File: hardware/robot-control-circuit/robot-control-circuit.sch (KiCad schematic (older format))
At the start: 41 parts, among them J1 CCRP5-EC2, J10 Testpoint GND, J11 Testpoint VDD, J12 Testpoint VCC, J13 CCRP5_Injections, J2 VL53L1-SATEL connector 1, J3 VL53L1-SATEL connector 2, J4 CCRP5-EC1, J5 VL53L1-SATEL connector 3, J6 VL53L1-SATEL connector 4, J7 CCRP5-EC3, J8 Bumper, Q1 BD235, Q2 BD235, Q3 BC548, U1 LM7805_TO220, U2 NodeMCU_1.0_(ESP-12E), U3 MCP23017_SP

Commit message: Added LEDs for generic signaling purposes.
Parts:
- added D?: Signal LED green, LED_THT:LED_D3.0mm, symbol Device:LED
- added D?: Signal LED yellow, LED_THT:LED_D3.0mm, symbol Device:LED
- added D?: Signal LED red, LED_THT:LED_D3.0mm, symbol Device:LED
- added D?: Signal LED blue, LED_THT:LED_D3.0mm, symbol Device:LED
- added R? (x3): 1k, Resistor_THT:R_Axial_DIN0204_L3.6mm_D1.6mm_P2.54mm_Vertical, symbol Device:R
- added R?: 0, Resistor_THT:R_Axial_DIN0204_L3.6mm_D1.6mm_P2.54mm_Vertical, symbol Device:R
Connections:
- net GND: now also D?.1 (K), D?.1 (K), D?.1 (K), D?.1 (K)
- net LED_GREEN: now reaches J13.7 (Pin_7), U3.3 (GPB2)
- net LED_GREEN: now also R?.2
- net LED_YELLOW: now reaches J13.8 (Pin_8), U3.4 (GPB3)
- net LED_YELLOW: now also R?.2
- net LED_RED: now reaches J13.9 (Pin_9), U3.5 (GPB4)
- net LED_RED: now also R?.2
- net LED_BLUE: now reaches J13.10 (Pin_10), U3.6 (GPB5)
- net LED_BLUE: now also R?.2
- new net: D?.2 (A), R?.1 (x4)
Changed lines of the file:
@@
 	4800 1150 5400 1150
 NoConn ~ 5350 1700
+$Comp
+L Device:LED D?
+U 1 1 618B38D5
+P 1550 4000
+F 0 "D?" V 1589 3883 50  0000 R CNN
+F 1 "Signal LED green" H 1500 3850 50  0000 R CNN
+F 2 "LED_THT:LED_D3.0mm" H 1550 4000 50  0001 C CNN
+F 3 "~" H 1550 4000 50  0001 C CNN
+	1    1550 4000
+	-1   0    0    1
+$EndComp
+$Comp
+L Device:R R?
+U 1 1 618B95BC
+P 1250 4000
+F 0 "R?" H 1320 4046 50  0000 L CNN
+F 1 "1k" H 1320 3955 50  0000 L CNN
+F 2 "Resistor_THT:R_Axial_DIN0204_L3.6mm_D1.6mm_P2.54mm_Vertical" V 1180 4000 50  0001 C CNN
+F 3 "~" H 1250 4000 50  0001 C CNN
+	1    1250 4000
+	0    1    1    0
+$EndComp
+$Comp
+L Device:LED D?
+U 1 1 618EC6EC
+P 1550 4350
+F 0 "D?" V 1589 4233 50  0000 R CNN
+F 1 "Signal LED yellow" H 1500 4200 50  0000 R CNN
+F 2 "LED_THT:LED_D3.0mm" H 1550 4350 50  0001 C CNN
+F 3 "~" H 1550 4350 50  0001 C CNN
+	1    1550 4350
+	-1   0    0    1
+$EndComp
+$Comp
+L Device:R R?
+U 1 1 618EC6F2
+P 1250 4350
+F 0 "R?" H 1320 4396 50  0000 L CNN
+F 1 "1k" H 1320 4305 50  0000 L CNN
+F 2 "Resistor_THT:R_Axial_DIN0204_L3.6mm_D1.6mm_P2.54mm_Vertical" V 1180 4350 50  0001 C CNN
+F 3 "~" H 1250 4350 50  0001 C CNN
+	1    1250 4350
+	0    1    1    0
+$EndComp
+$Comp
+L Device:LED D?
+U 1 1 618EF321
+P 1550 4700
+F 0 "D?" V 1589 4583 50  0000 R CNN
+F 1 "Signal LED red" H 1500 4550 50  0000 R CNN
+F 2 "LED_THT:LED_D3.0mm" H 1550 4700 50  0001 C CNN
+F 3 "~" H 1550 4700 50  0001 C CNN
+	1    1550 4700
+	-1   0    0    1
+$EndComp
+$Comp
+L Device:R R?
+U 1 1 618EF327
+P 1250 4700
+F 0 "R?" H 1320 4746 50  0000 L CNN
+F 1 "1k" H 1320 4655 50  0000 L CNN
+F 2 "Resistor_THT:R_Axial_DIN0204_L3.6mm_D1.6mm_P2.54mm_Vertical" V 1180 4700 50  0001 C CNN
+F 3 "~" H 1250 4700 50  0001 C CNN
+	1    1250 4700
+	0    1    1    0
+$EndComp
+$Comp
+L Device:LED D?
+U 1 1 618F1222
+P 1550 5050
+F 0 "D?" V 1589 4933 50  0000 R CNN
+F 1 "Signal LED blue" H 1500 4900 50  0000 R CNN
+F 2 "LED_THT:LED_D3.0mm" H 1550 5050 50  0001 C CNN
+F 3 "~" H 1550 5050 50  0001 C CNN
+	1    1550 5050
+	-1   0    0    1
+$EndComp
+$Comp
+L Device:R R?
+U 1 1 618F1228
+P 1250 5050
+F 0 "R?" H 1320 5096 50  0000 L CNN
+F 1 "0" H 1320 5005 50  0000 L CNN
+F 2 "Resistor_THT:R_Axial_DIN0204_L3.6mm_D1.6mm_P2.54mm_Vertical" V 1180 5050 50  0001 C CNN
+F 3 "~" H 1250 5050 50  0001 C CNN
+	1    1250 5050
+	0    1    1    0
+$EndComp
+$Comp
+L power:GND #PWR?
+U 1 1 619002BD
+P 1800 5200
+F 0 "#PWR?" H 1800 4950 50  0001 C CNN
+F 1 "GND" H 1805 5027 50  0000 C CNN
+F 2 "" H 1800 5200 50  0001 C CNN
+F 3 "" H 1800 5200 50  0001 C CNN
+	1    1800 5200
+	1    0    0    -1
+$EndComp
+Wire Wire Line
+	1800 5200 1800 5050
+Wire Wire Line
+	1800 4000 1700 4000
+Wire Wire Line
+	1700 4350 1800 4350
+Connection ~ 1800 4350
+Wire Wire Line
+	1800 4350 1800 4000
+Wire Wire Line
+	1700 4700 1800 4700
+Connection ~ 1800 4700
+Wire Wire Line
+	1800 4700 1800 4350
+Wire Wire Line
+	1700 5050 1800 5050
+Connection ~ 1800 5050
+Wire Wire Line
+	1800 5050 1800 4700
+Wire Wire Line
+	650  4000 1100 4000
+Text Label 650  4000 0    50   ~ 0
+LED_GREEN
+Wire Wire Line
+	1100 4350 650  4350
+Wire Wire Line
+	1100 4700 650  4700
+Wire Wire Line
+	1100 5050 650  5050
+Text Label 650  4350 0    50   ~ 0
+LED_YELLOW
+Text Label 650  4700 0    50   ~ 0
+LED_RED
+Text Label 650  5050 0    50   ~ 0
+LED_BLUE
+Text Label 8750 3400 0    50   ~ 0
+LED_GREEN
+Text Label 8750 3500 0    50   ~ 0
+LED_YELLOW
+Text Label 8750 3600 0    50   ~ 0
+LED_RED
+Text Label 8750 3700 0    50   ~ 0
+LED_BLUE
 $EndSCHEMATC

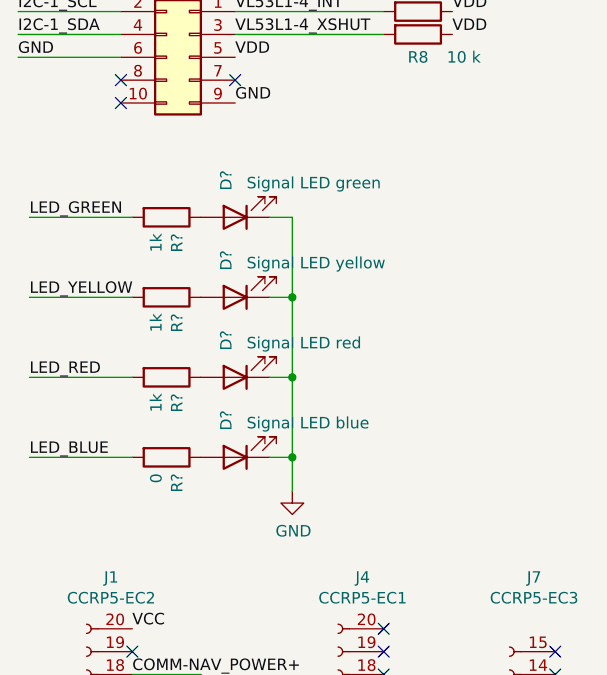
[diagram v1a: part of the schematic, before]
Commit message: Connected new LEDs.
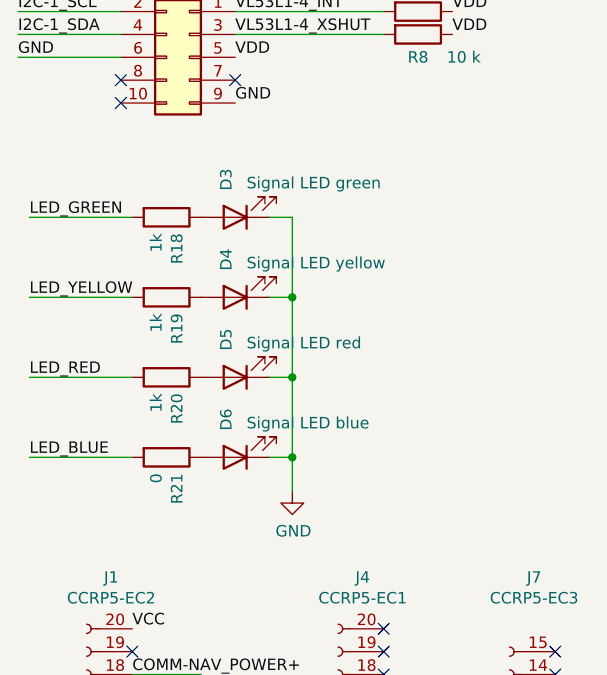
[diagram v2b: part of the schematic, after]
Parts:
- gave numbers to parts that had none: 8
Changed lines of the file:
@@
 NoConn ~ 5350 1700
 $Comp
-L Device:LED D?
+L Device:LED D3
 U 1 1 618B38D5
 P 1550 4000
-F 0 "D?" V 1589 3883 50  0000 R CNN
+F 0 "D3" V 1589 3883 50  0000 R CNN
 F 1 "Signal LED green" H 1500 3850 50  0000 R CNN
 F 2 "LED_THT:LED_D3.0mm" H 1550 4000 50  0001 C CNN
@@
 $EndComp
 $Comp
-L Device:R R?
+L Device:R R18
 U 1 1 618B95BC
 P 1250 4000
-F 0 "R?" H 1320 4046 50  0000 L CNN
+F 0 "R18" H 1320 4046 50  0000 L CNN
 F 1 "1k" H 1320 3955 50  0000 L CNN
 F 2 "Resistor_THT:R_Axial_DIN0204_L3.6mm_D1.6mm_P2.54mm_Vertical" V 1180 4000 50  0001 C CNN
@@
 $EndComp
 $Comp
-L Device:LED D?
+L Device:LED D4
 U 1 1 618EC6EC
 P 1550 4350
-F 0 "D?" V 1589 4233 50  0000 R CNN
+F 0 "D4" V 1589 4233 50  0000 R CNN
 F 1 "Signal LED yellow" H 1500 4200 50  0000 R CNN
 F 2 "LED_THT:LED_D3.0mm" H 1550 4350 50  0001 C CNN
@@
 $EndComp
 $Comp
-L Device:R R?
+L Device:R R19
 U 1 1 618EC6F2
 P 1250 4350
-F 0 "R?" H 1320 4396 50  0000 L CNN
+F 0 "R19" H 1320 4396 50  0000 L CNN
 F 1 "1k" H 1320 4305 50  0000 L CNN
 F 2 "Resistor_THT:R_Axial_DIN0204_L3.6mm_D1.6mm_P2.54mm_Vertical" V 1180 4350 50  0001 C CNN
@@
 $EndComp
 $Comp
-L Device:LED D?
+L Device:LED D5
 U 1 1 618EF321
 P 1550 4700
-F 0 "D?" V 1589 4583 50  0000 R CNN
+F 0 "D5" V 1589 4583 50  0000 R CNN
 F 1 "Signal LED red" H 1500 4550 50  0000 R CNN
 F 2 "LED_THT:LED_D3.0mm" H 1550 4700 50  0001 C CNN
@@
 $EndComp
 $Comp
-L Device:R R?
+L Device:R R20
 U 1 1 618EF327
 P 1250 4700
-F 0 "R?" H 1320 4746 50  0000 L CNN
+F 0 "R20" H 1320 4746 50  0000 L CNN
 F 1 "1k" H 1320 4655 50  0000 L CNN
 F 2 "Resistor_THT:R_Axial_DIN0204_L3.6mm_D1.6mm_P2.54mm_Vertical" V 1180 4700 50  0001 C CNN
@@
 $EndComp
 $Comp
-L Device:LED D?
+L Device:LED D6
 U 1 1 618F1222
 P 1550 5050
-F 0 "D?" V 1589 4933 50  0000 R CNN
+F 0 "D6" V 1589 4933 50  0000 R CNN
 F 1 "Signal LED blue" H 1500 4900 50  0000 R CNN
 F 2 "LED_THT:LED_D3.0mm" H 1550 5050 50  0001 C CNN
@@
 $EndComp
 $Comp
-L Device:R R?
+L Device:R R21
 U 1 1 618F1228
 P 1250 5050
-F 0 "R?" H 1320 5096 50  0000 L CNN
+F 0 "R21" H 1320 5096 50  0000 L CNN
 F 1 "0" H 1320 5005 50  0000 L CNN
 F 2 "Resistor_THT:R_Axial_DIN0204_L3.6mm_D1.6mm_P2.54mm_Vertical" V 1180 5050 50  0001 C CNN
@@
 $EndComp
 $Comp
-L power:GND #PWR?
+L power:GND #PWR02
 U 1 1 619002BD
 P 1800 5200
-F 0 "#PWR?" H 1800 4950 50  0001 C CNN
+F 0 "#PWR02" H 1800 4950 50  0001 C CNN
 F 1 "GND" H 1805 5027 50  0000 C CNN
 F 2 "" H 1800 5200 50  0001 C CNN
